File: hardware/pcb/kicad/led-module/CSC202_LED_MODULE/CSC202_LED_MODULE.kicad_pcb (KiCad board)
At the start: 2 copper layers, 45 x 86 mm, 28 parts, among them J1 SPI TAP, J2 PWR_IF, J3 LED_IF, J4 SPI_IF, J6 EN_IF, SW1 SPI↔BUF, U1 CA56-12SEKWA, U2 74HC244, U3 74HC595

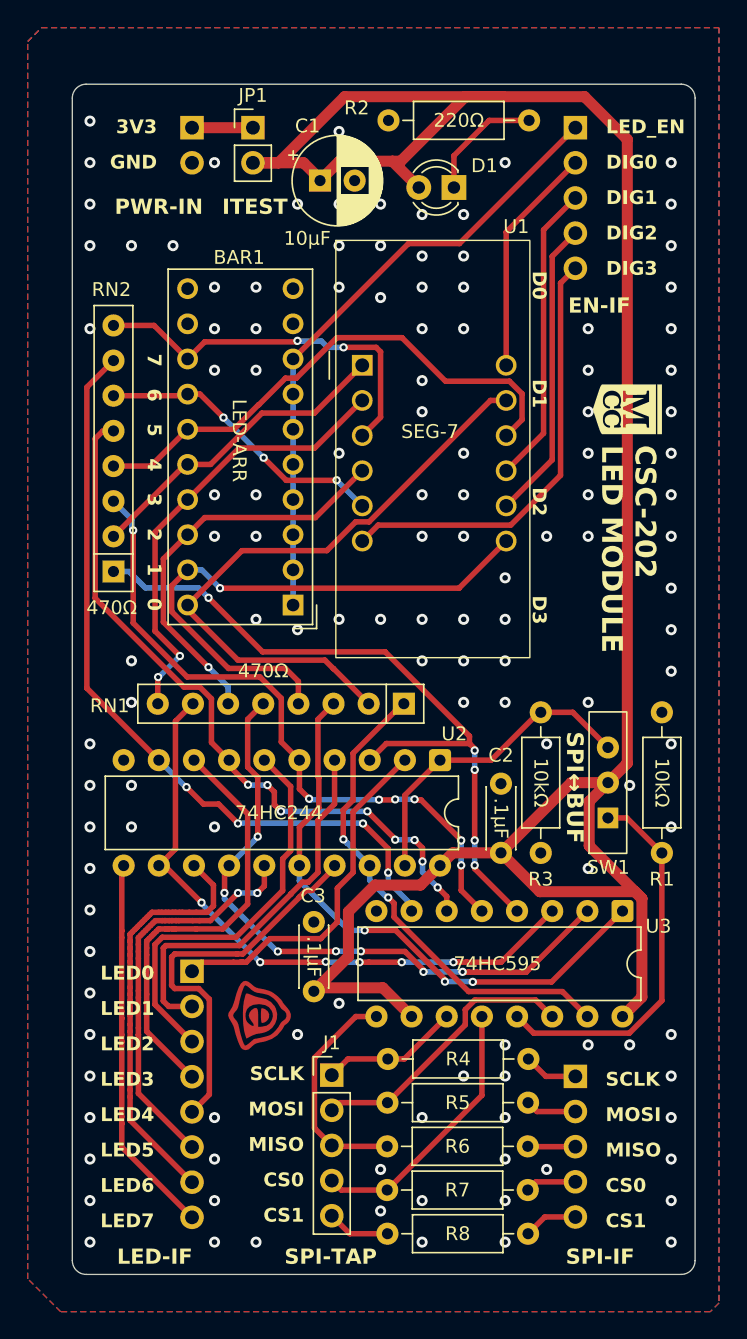
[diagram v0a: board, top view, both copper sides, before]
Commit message: added reverse polarity protection and included bottom assy in outputs
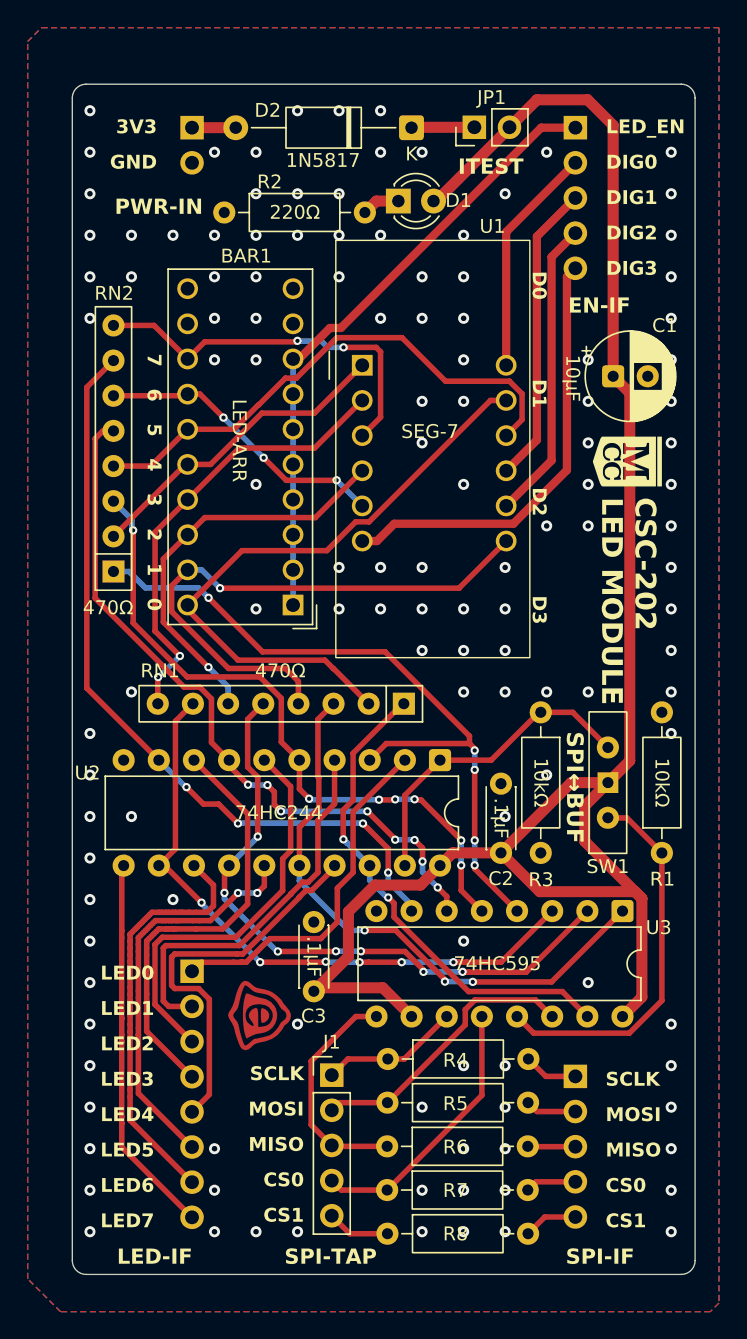
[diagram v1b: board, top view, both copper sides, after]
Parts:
- added D2: 1N5817, led-module:D_A-405_P12.70mm_Horizontal, F.Cu at (142.6, 53.4)
- D1: value PWR_LED -> PWR
- J1: value SPI TAP -> SPI-TAP
- J2: value PWR_IF -> PWR-IN
- J3: value LED_IF -> LED-IF
- J4: value SPI_IF -> SPI-IF
- J5: renamed from J6; value EN_IF -> EN-IF
- JP1: value TEST_PT -> TEST-PT
- SW1: value SPI↔BUF -> BUF↔SPI
- moved C1 25.5 mm to (157.2, 71.4)
- moved JP1 16.0 mm to (147.1, 53.4), turned to 90 degrees
- moved R2 13.6 mm to (129.1, 59.5)
- moved D1 4.13 mm to (141.6, 58.7), turned to 0 degrees
- moved G*** 3.77 mm to (158.2, 77.5)
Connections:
- J2 pad 1: Net-(J2-Pin_1) -> Net-(D2-A)
- JP1 pad 1: Net-(J2-Pin_1) -> Net-(D2-K)
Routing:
- net +3V3: track 169.8 -> 134.3 mm
- net Net-(D1-K): track 8.79 -> 2.76 mm
- net Net-(D2-K): track 0.00 -> 4.51 mm
- net Net-(J2-Pin_1): track 4.40 -> 0.00 mm
- net Net-(D2-A): track 0.00 -> 3.16 mm
- net GND: vias 128 -> 127
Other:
- board text added: "1N5817"
- board text added: "{ "ViaStitching": "0.2", "stitch_zone_0": { "HSpacing": "3", "VSpacing": "3", "HOffset": "1.5", "VOffset": "0", "Clearance": ".2", "Randomize": false } }"

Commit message: update LED module KiCad design
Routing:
- net GND: vias 127 -> 124
- net /MISO_EXT: vias 0 -> 1
- net /LED_R1: vias 1 -> 2
- net /CS0_EXT: vias 0 -> 1
